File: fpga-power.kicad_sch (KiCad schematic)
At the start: 76 parts

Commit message: Added EN pullup for TPS54561 to avoid disabling by touch
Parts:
- C100, C104, C114, C116, C118, C47, C51, C55, C57, C59, C61, C63, C65, C66, C67, C69, C70, C71, C73, C74, C75, C77, C78, C79, C81, C82, C83, C84, C85, C87, C88, C89, C91, C92, C93, C95, C96, C97, C98: value (none) -> C_100n_0201; footprint (none) -> ddr5-testboard-footprints:0201-res
- C101, C106, C107, C108, C109, C110, C111, C113, C115, C117, C48, C50, C52, C54, C56, C58, C62, C68, C72, C76, C80, C86, C90, C94, C99: value (none) -> C_4u7_0402; footprint (none) -> ddr5-testboard-footprints:0402-cap
- C102, C105: value (none) -> C_330u_KEMET_D; footprint (none) -> ddr5-testboard-footprints:KEMET_D
- C103, C60, C64: value (none) -> C_47u_0603; footprint (none) -> ddr5-testboard-footprints:0603-cap
- C112: value (none) -> C_100u_KEMET_A; footprint (none) -> ddr5-testboard-footprints:KEMET_A
- C119, C120, C121, C49, C53: renamed from C?; value (none) -> C_47u_0603; footprint (none) -> ddr5-testboard-footprints:0603-cap
- U8: value (none) -> XC7K160T-FFG676; footprint (none) -> ddr5-testboard-footprints:BGA676C100P26X26_2700X2700X254

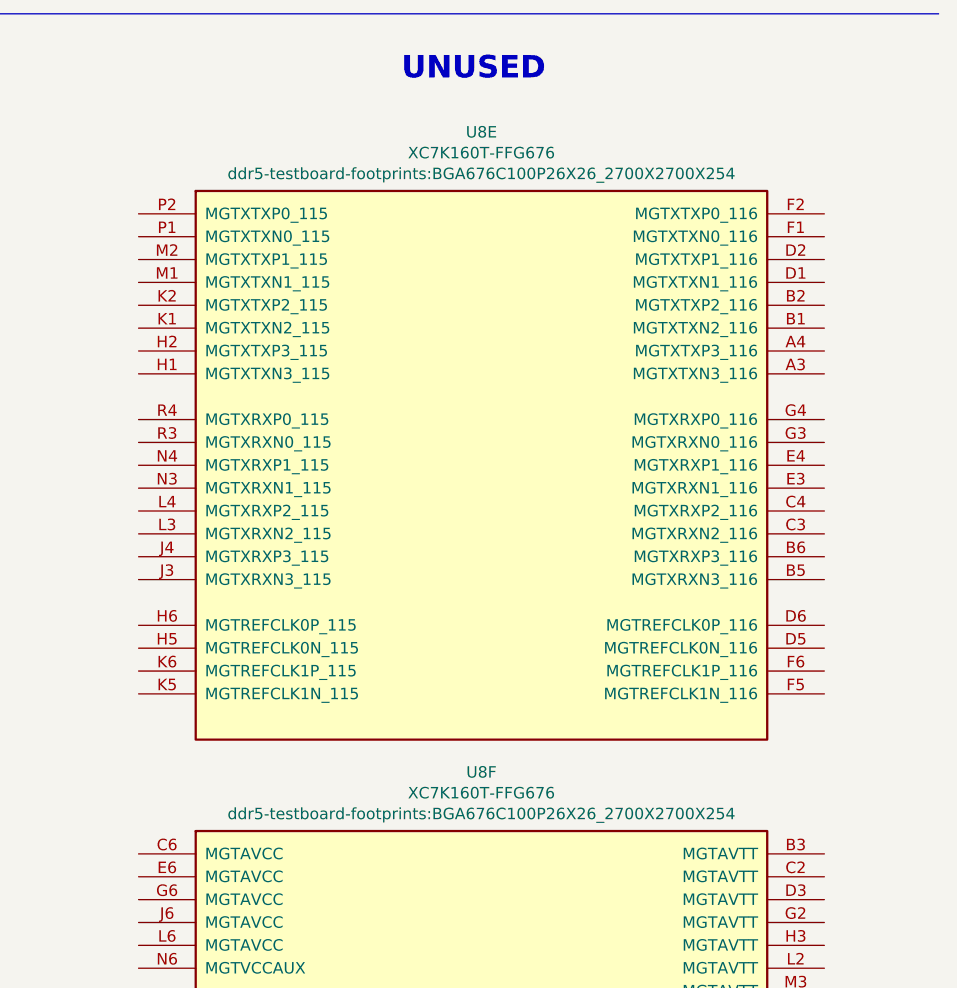
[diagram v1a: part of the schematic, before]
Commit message: Update FPGA footprint reference
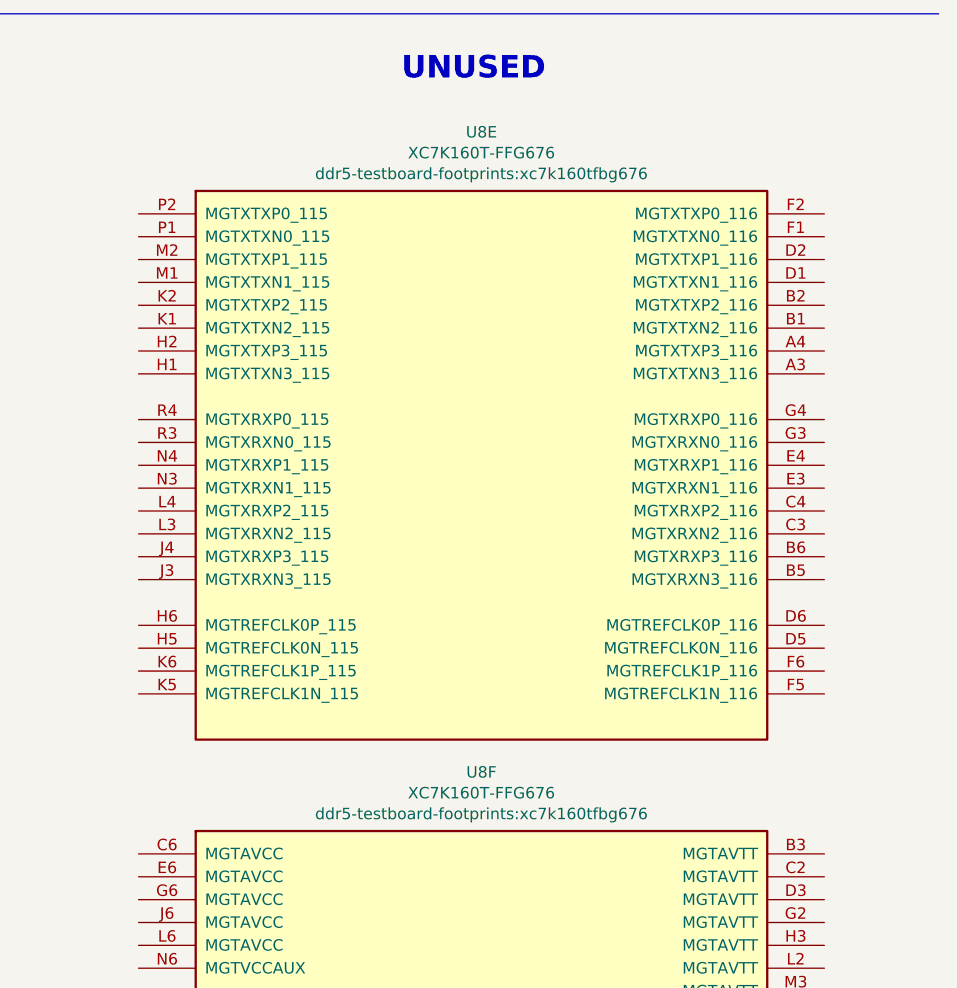
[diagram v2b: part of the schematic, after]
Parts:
- U8: footprint ddr5-testboard-footprints:BGA676C100P26X26_2700X2700X254 -> ddr5-testboard-footprints:xc7k160tfbg676
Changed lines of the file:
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@@
     (pin "1")
   )
-  (symbol (lib_id "ddr5-testboard:XC7K160T-FFG676") (at 357.505 173.355 0) (unit 5)
+  (symbol (lib_name "XC7K160T-FFG676_2") (lib_id "ddr5-testboard:XC7K160T-FFG676") (at 357.505 173.355 0) (unit 5)
     (in_bom yes) (on_board yes)
     (property "Reference" "U8" (id 0) (at 357.505 136.3472 0))
     (property "Value" "XC7K160T-FFG676" (id 1) (at 357.505 138.6586 0))
-    (property "Footprint" "ddr5-testboard-footprints:BGA676C100P26X26_2700X2700X254" (id 2) (at 357.505 140.97 0))
+    (property "Footprint" "ddr5-testboard-footprints:xc7k160tfbg676" (id 2) (at 357.505 140.97 0))
     (property "Datasheet" "" (id 3) (at 357.505 173.355 0))
     (pin "AA21")
@@
     (property "Reference" "U8" (id 0) (at 357.505 207.4672 0))
     (property "Value" "XC7K160T-FFG676" (id 1) (at 357.505 209.7786 0))
-    (property "Footprint" "ddr5-testboard-footprints:BGA676C100P26X26_2700X2700X254" (id 2) (at 357.505 212.09 0))
+    (property "Footprint" "ddr5-testboard-footprints:xc7k160tfbg676" (id 2) (at 357.505 212.09 0))
     (property "Datasheet" "" (id 3) (at 357.505 229.235 0))
     (pin "AA21")
@@
     (pin "Y9")
   )
-  (symbol (lib_id "ddr5-testboard:XC7K160T-FFG676") (at 261.62 161.925 0) (unit 8)
+  (symbol (lib_name "XC7K160T-FFG676_1") (lib_id "ddr5-testboard:XC7K160T-FFG676") (at 261.62 161.925 0) (unit 8)
     (in_bom yes) (on_board yes)
     (property "Reference" "U8" (id 0) (at 261.62 53.7972 0))
     (property "Value" "XC7K160T-FFG676" (id 1) (at 261.62 56.1086 0))
-    (property "Footprint" "ddr5-testboard-footprints:BGA676C100P26X26_2700X2700X254" (id 2) (at 261.62 58.42 0)
+    (property "Footprint" "ddr5-testboard-footprints:xc7k160tfbg676" (id 2) (at 261.62 58.42 0)
       (effects (font (size 1.27 1.27)) hide)
     )

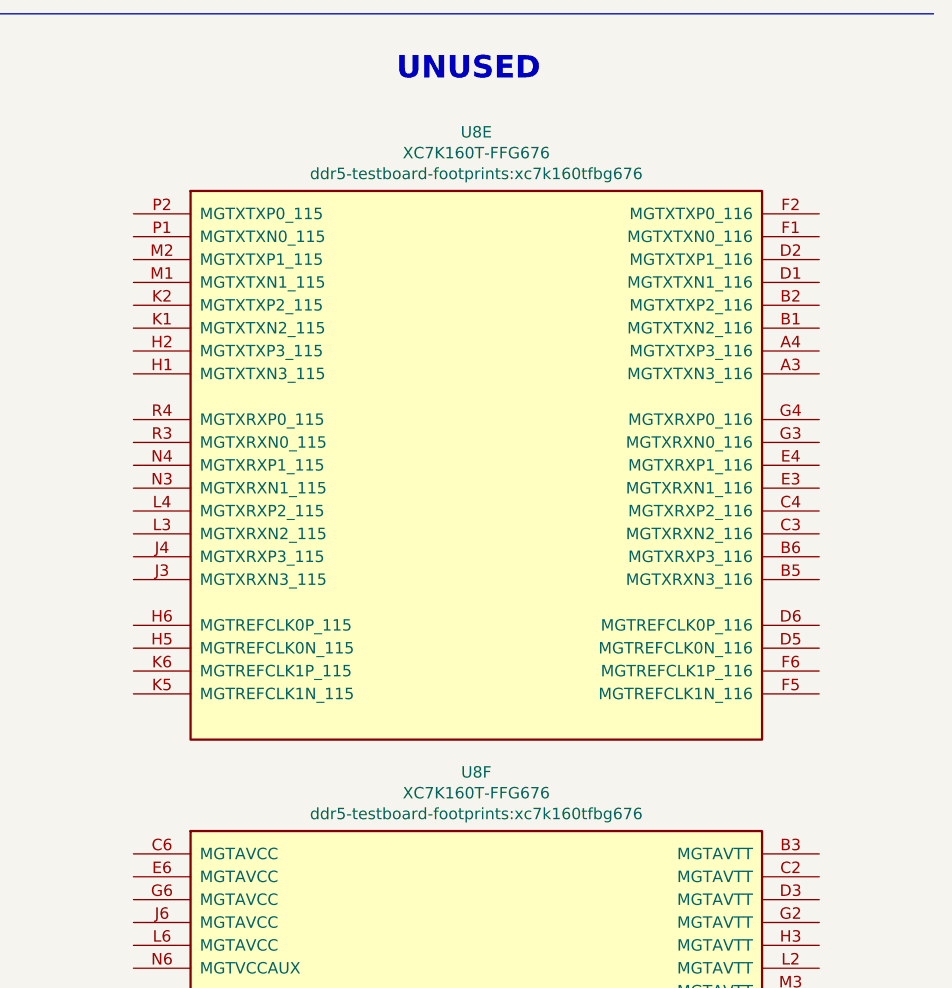
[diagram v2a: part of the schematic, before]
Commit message: Update naming convention
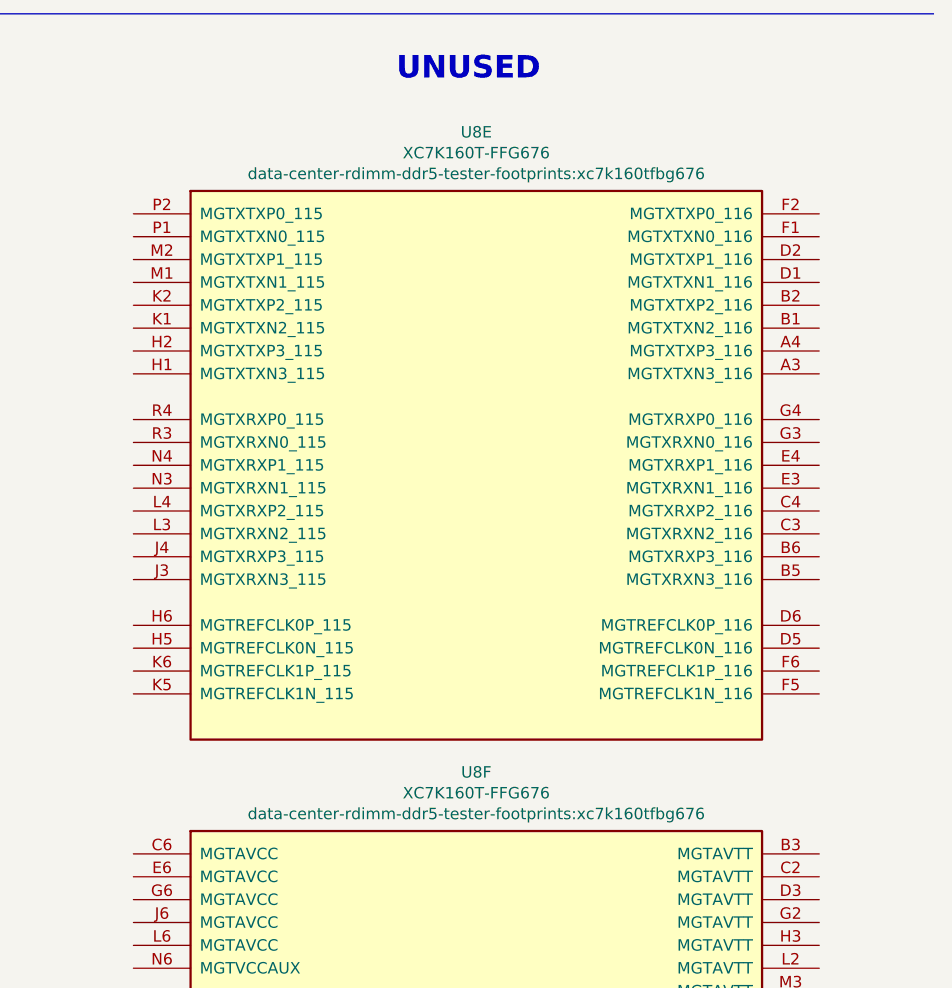
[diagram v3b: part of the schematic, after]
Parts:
- C100, C104, C114, C116, C118, C47, C51, C55, C57, C59, C61, C63, C65, C66, C67, C69, C70, C71, C73, C74, C75, C77, C78, C79, C81, C82, C83, C84, C85, C87, C88, C89, C91, C92, C93, C95, C96, C97, C98: footprint ddr5-testboard-footprints:0201-res -> data-center-rdimm-ddr5-tester-footprints:0201-res; symbol ddr5-testboard:C_100n_0201 -> data-center-rdimm-ddr5-tester:C_100n_0201
- C101, C106, C107, C108, C109, C110, C111, C113, C115, C117, C48, C50, C52, C54, C56, C58, C62, C68, C72, C76, C80, C86, C90, C94, C99: footprint ddr5-testboard-footprints:0402-cap -> data-center-rdimm-ddr5-tester-footprints:0402-cap; symbol ddr5-testboard:C_4u7_0402 -> data-center-rdimm-ddr5-tester:C_4u7_0402
- C102, C105: footprint ddr5-testboard-footprints:KEMET_D -> data-center-rdimm-ddr5-tester-footprints:KEMET_D; symbol ddr5-testboard:C_330u_KEMET_D -> data-center-rdimm-ddr5-tester:C_330u_KEMET_D
- C103, C119, C120, C121, C49, C53, C60, C64: footprint ddr5-testboard-footprints:0603-cap -> data-center-rdimm-ddr5-tester-footprints:0603-cap; symbol ddr5-testboard:C_47u_0603 -> data-center-rdimm-ddr5-tester:C_47u_0603
- C112: footprint ddr5-testboard-footprints:KEMET_A -> data-center-rdimm-ddr5-tester-footprints:KEMET_A; symbol ddr5-testboard:C_100u_KEMET_A -> data-center-rdimm-ddr5-tester:C_100u_KEMET_A
- U8: footprint ddr5-testboard-footprints:xc7k160tfbg676 -> data-center-rdimm-ddr5-tester-footprints:xc7k160tfbg676; symbol ddr5-testboard:XC7K160T-FFG676 -> data-center-rdimm-ddr5-tester:XC7K160T-FFG676
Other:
- title: DDR5 Tester -> Data Center RDIMM DDR5 Tester

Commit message: Introduce component standarization
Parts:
- removed unit 6 of U8
- C100, C104, C114, C116, C118, C47, C51, C55, C57, C59, C61, C63, C65, C66, C67, C69, C70, C71, C73, C74, C75, C77, C78, C79, C81, C82, C83, C84, C85, C87, C88, C89, C91, C92, C93, C95, C96, C97, C98: footprint data-center-rdimm-ddr5-tester-footprints:0201-res -> data-center-rdimm-ddr5-tester-footprints:C_0201; Author (none) -> Antmicro; License (none) -> Apache-2.0; Manufacturer YAGEO -> Yaego
- C101, C106, C107, C108, C109, C110, C111, C113, C115, C117, C48, C50, C52, C54, C56, C58, C62, C68, C72, C76, C80, C86, C90, C94, C99: footprint data-center-rdimm-ddr5-tester-footprints:0402-cap -> data-center-rdimm-ddr5-tester-footprints:C_0402_1005Metric; Author (none) -> Antmicro; License (none) -> Apache-2.0; Manufacturer MURATA -> Murata
- C102, C105: Author (none) -> Antmicro; License (none) -> Apache-2.0
- C103, C119, C120, C121, C49, C53, C60, C64: footprint data-center-rdimm-ddr5-tester-footprints:0603-cap -> data-center-rdimm-ddr5-tester-footprints:C_0603_1608Metric; Author (none) -> Antmicro; License (none) -> Apache-2.0; Manufacturer MURATA -> Murata
- C112: Author (none) -> Antmicro; License (none) -> Apache-2.0; Manufacturer VISHAY -> Vishay
- U8: footprint data-center-rdimm-ddr5-tester-footprints:xc7k160tfbg676 -> data-center-rdimm-ddr5-tester-footprints:BGA-676_27x27mm_Layout26x26_P1X1mm; Author (none) -> Antmicro; License (none) -> Apache-2.0; MPN (none) -> XC7K160T-FFG676; Manufacturer (none) -> Xilinx
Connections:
- net 1V0_SYS: now also C55.2, C63.2, C84.2; no longer C55.1, C63.1, C84.1
- net 1V1_SYS: now also C61.2, C69.2; no longer C61.1, C69.1
- net 1V8_SYS: now also C60.2; no longer C60.1
- net 3V3_SYS: now also C54.2, C76.2; no longer C54.1, C76.1
- net GND: now also C54.1, C55.1, C60.1, C61.1, C63.1, C69.1, C76.1, C84.1; no longer C54.2, C55.2, C60.2, C61.2, C63.2, C69.2, C76.2, C84.2
- new net: U8.B3 (MGTAVTT), U8.C2 (MGTAVTT), U8.D3 (MGTAVTT), U8.G2 (MGTAVTT), U8.H3 (MGTAVTT), U8.L2 (MGTAVTT), U8.M3 (MGTAVTT)
- new net: U8.C6 (MGTAVCC), U8.E6 (MGTAVCC), U8.G6 (MGTAVCC), U8.J6 (MGTAVCC), U8.L6 (MGTAVCC)
- no-connect marks 0 -> 45
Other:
- moved on the sheet: C100, C101, C103, C104, C106, C107, C108, C109, C110, C111, C113, C114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

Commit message: [#55296] component update
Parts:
- U8: Manufacturer Xilinx -> AMD-Xilinx
